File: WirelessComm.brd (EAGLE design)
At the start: 41.9 x 53.3 mm, 28 parts

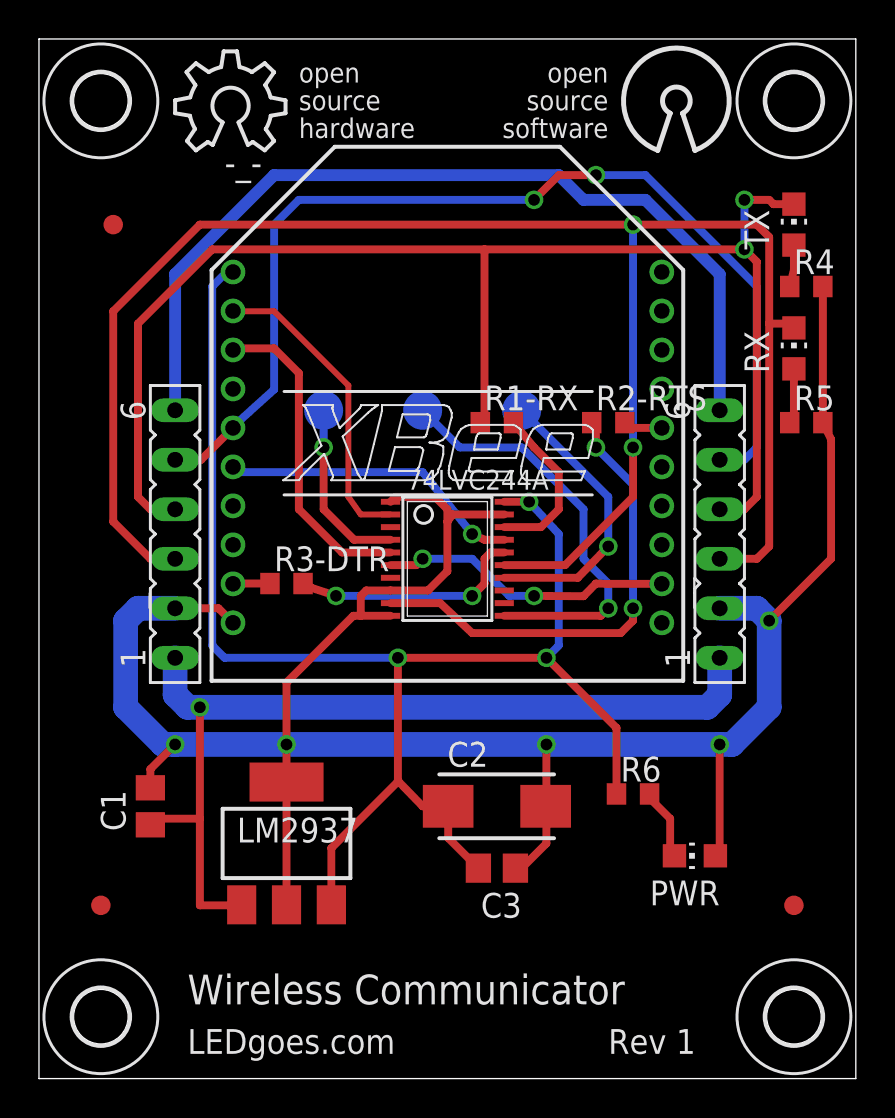
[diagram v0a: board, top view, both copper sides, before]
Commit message: First Production Revision
Passed design review check 2/25/14.  Rotated bee 90 degrees to keep this
board's size the same as the others.
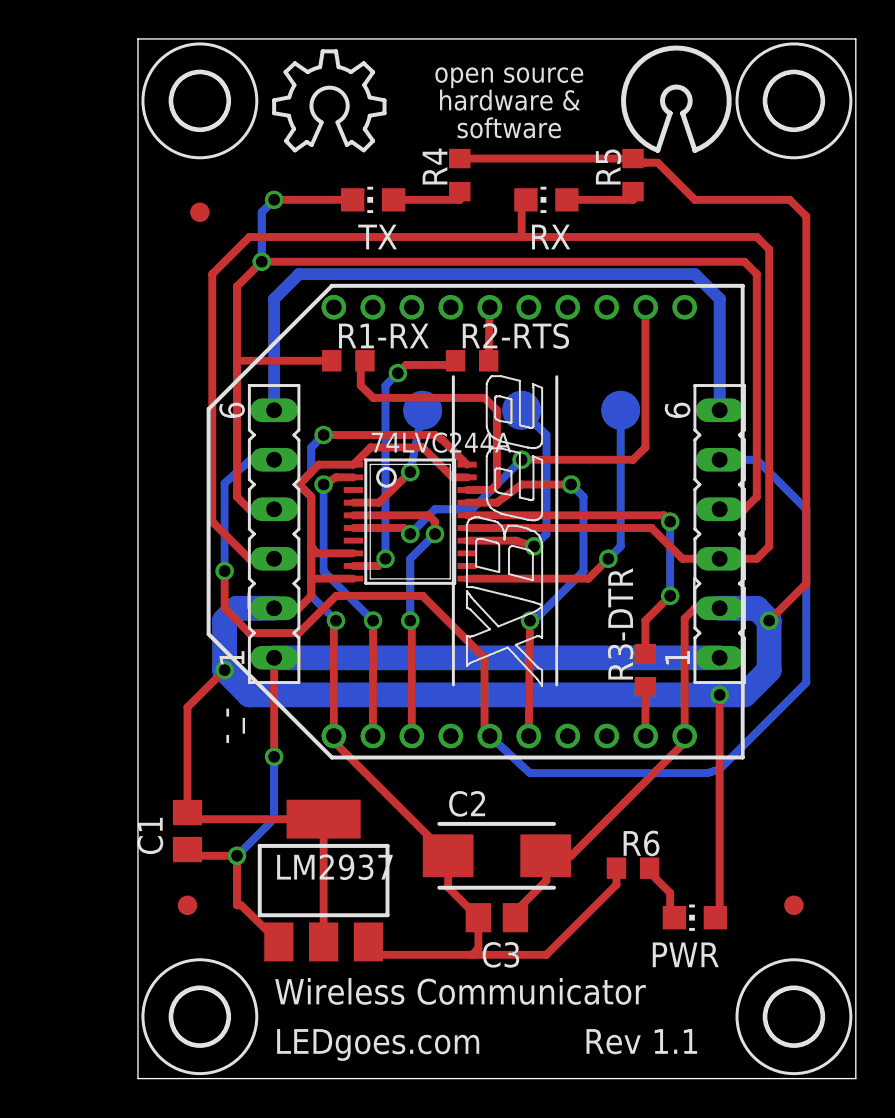
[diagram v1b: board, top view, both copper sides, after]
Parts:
- R4, R5, R6: value 47 -> 330
- moved TX 21.6 mm to (18.4, 42.5), turned to 90 degrees
- moved R3-DTR 18.9 mm to (32.4, 18.4), turned to 90 degrees
- moved R4 18.7 mm to (22.9, 43.8), turned to 90 degrees
- moved R5 15.5 mm to (31.8, 43.8), turned to 90 degrees
- moved RX 14.8 mm to (27.3, 42.5), turned to 90 degrees
- moved /RTS 10.2 mm to (31.1, 31.8)
- moved R1-RX 8.26 mm to (17.1, 34.3)
- moved R2-RTS 7.67 mm to (23.5, 34.3)
- moved E$1 5.08 mm to (13.3, 45.1)
- moved E$3 5.08 mm to (9.53, 47.6)
- moved E$4 5.08 mm to (9.53, 0.64)
- moved _ 5.08 mm to (13.3, 25.4)
- moved /DTR 5.08 mm to (21.0, 31.8)
- moved -_- 4.96 mm to (25.4, 26.0), turned to 90 degrees
- moved E$6 4.49 mm to (9.53, 41.9)
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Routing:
- net GND: track 126.8 -> 158.0 mm, vias 5 -> 3
- net S$3: track 76.8 -> 54.7 mm, vias 3 -> 2
- net S$23: track 93.0 -> 80.1 mm, vias 2 -> 0
- net S$1: track 46.1 -> 35.3 mm
- net S$13: track 24.4 -> 14.8 mm
- net S$10: track 15.1 -> 24.4 mm
- net S$2: track 53.6 -> 62.8 mm, vias 2 -> 1
- net VCC: track 50.3 -> 41.9 mm, vias 1 -> 2
- net S$25: track 73.2 -> 66.4 mm
- net S$7: track 8.53 -> 14.4 mm
- net S$4: track 21.5 -> 15.5 mm
- net S$15: track 12.1 -> 17.8 mm
- net S$16: track 15.8 -> 20.1 mm, vias 1 -> 2
- net S$5: track 14.8 -> 11.3 mm
- net S$17: track 9.16 -> 6.79 mm
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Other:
- board size 41.9 x 53.3 mm -> 36.8 x 53.3 mm
- board text added: "Rev 1.1"
- board text added: "open source hardware & software"
- board text removed: "Rev 1"
- board text removed: "open source hardware"
- board text removed: "open source software"

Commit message: Slight changes made to Rev 1 before production
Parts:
- turned PWR to 270 degrees
- turned RX to 270 degrees
- turned TX to 270 degrees
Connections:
- net GND: now also PWR.C; no longer PWR.A
- net S$11: now also PWR.A; no longer PWR.C
- net S$14: now also TX.C; no longer TX.A
- net S$18: now also RX.C; no longer RX.A
- net S$23: now also RX.A; no longer RX.C
- net S$25: now also TX.A; no longer TX.C
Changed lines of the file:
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@@
 <wire x1="43.18" y1="50.8" x2="6.35" y2="50.8" width="0" layer="20"/>
 <text x="13.335" y="-1.27" size="1.27" layer="25" font="vector">LEDgoes.com</text>
-<text x="10.16" y="17.78" size="0.8128" layer="26" font="vector" rot="MR90">VCC GND RX TX RST RIN</text>
+<text x="15.875" y="17.78" size="0.8128" layer="25" font="vector" rot="R90">VCC GND RX TX RST RIN</text>
 <text x="25.4" y="45.72" size="1.016" layer="25" font="vector" distance="40" align="bottom-center">open source
 hardware &amp;
@@
 <element name="E$2" library="holes" package="2,8" value="" x="40.005" y="47.625"/>
 <element name="E$5" library="holes" package="2,8" value="" x="40.005" y="0.635"/>
-<element name="-_-" library="maxstream" package="XBEE" value="" x="25.4" y="26.035" rot="R90"/>
-<element name="TX" library="led" package="CHIP-LED0805" value="" x="18.415" y="42.545" rot="R90"/>
-<element name="RX" library="led" package="CHIP-LED0805" value="" x="27.305" y="42.545" rot="R90"/>
-<element name="PWR" library="led" package="CHIP-LED0805" value="" x="34.925" y="5.715" rot="R90"/>
-<element name="74LVC244A" library="mcp2515" package="TSSOP20" value="" x="20.32" y="26.035" rot="R270"/>
-<element name="LM2937" library="v-reg" package="SOT223" value="" x="15.875" y="7.62"/>
-<element name="C1" library="eagle-ltspice" package="C0805" value="0.1uf" x="8.89" y="10.16" rot="R90"/>
-<element name="C3" library="eagle-ltspice" package="C0805" value="0.1uf" x="24.765" y="5.715" rot="R180"/>
-<element name="C2" library="resistor" package="CT6032" value="10uf" x="24.765" y="8.89"/>
-<element name="R3-DTR" library="eagle-ltspice" package="R0603" value="1k" x="32.385" y="18.415" rot="R90"/>
-<element name="R2-RTS" library="eagle-ltspice" package="R0603" value="1k" x="23.495" y="34.29"/>
-<element name="R1-RX" library="eagle-ltspice" package="R0603" value="1k" x="17.145" y="34.29"/>
-<element name="R4" library="eagle-ltspice" package="R0603" value="330" x="22.86" y="43.815" rot="R90"/>
-<element name="R5" library="eagle-ltspice" package="R0603" value="330" x="31.75" y="43.815" rot="R90"/>
-<element name="R6" library="eagle-ltspice" package="R0603" value="330" x="31.75" y="8.255"/>
+<element name="-_-" library="maxstream" package="XBEE" value="" x="25.4" y="26.035" smashed="yes" rot="R90">
+<attribute name="NAME" x="11.43" y="14.605" size="1.27" layer="25" rot="R90"/>
+<attribute name="VALUE" x="39.37" y="14.605" size="1.27" layer="27" rot="R90"/>
+</element>
+<element name="TX" library="led" package="CHIP-LED0805" value="" x="18.415" y="42.545" smashed="yes" rot="R270">
+<attribute name="NAME" x="17.78" y="43.815" size="1.016" layer="25" font="vector"/>
+<attribute name="VALUE" x="17.145" y="40.005" size="1.27" layer="27"/>
+</element>
+<element name="RX" library="led" package="CHIP-LED0805" value="" x="27.305" y="42.545" smashed="yes" rot="R270">
+<attribute name="NAME" x="26.67" y="40.64" size="1.016" layer="25" font="vector"/>
+<attribute name="VALUE" x="26.035" y="40.005" size="1.27" layer="27"/>
+</element>
+<element name="PWR" library="led" package="CHIP-LED0805" value="" x="34.925" y="5.715" smashed="yes" rot="R270">
+<attribute name="NAME" x="33.655" y="6.985" size="1.016" layer="25" font="vector"/>
+<attribute name="VALUE" x="33.655" y="3.175" size="1.27" layer="27"/>
+</element>
+<element name="74LVC244A" library="mcp2515" package="TSSOP20" value="" x="20.32" y="26.035" smashed="yes" rot="R270">
+<attribute name="NAME" x="18.2372" y="29.5806" size="1.016" layer="25" font="vector" ratio="10"/>
+<attribute name="VALUE" x="18.2372" y="21.4988" size="1.016" layer="27" ratio="10"/>
+</element>
+<element name="LM2937" library="v-reg" package="SOT223" value="" x="15.875" y="7.62" smashed="yes">
+<attribute name="NAME" x="13.335" y="12.1158" size="1.016" layer="25" font="vector"/>
+<attribute name="VALUE" x="13.335" y="6.2992" size="1.27" layer="27"/>
+</element>
+<element name="C1" library="eagle-ltspice" package="C0805" value="0.1uf" x="8.89" y="10.16" smashed="yes" rot="R90">
+<attribute name="NAME" x="7.62" y="9.525" size="1.016" layer="25" font="vector" rot="R90"/>
+<attribute name="VALUE" x="11.43" y="8.89" size="1.016" layer="27" font="vector" rot="R90"/>
+</element>
+<element name="C3" library="eagle-ltspice" package="C0805" value="0.1uf" x="24.765" y="5.715" smashed="yes" rot="R180">
+<attribute name="NAME" x="26.035" y="4.445" size="1.016" layer="25" font="vector" rot="R180"/>
+<attribute name="VALUE" x="26.035" y="8.255" size="1.016" layer="27" font="vector" rot="R180"/>
+</element>
+<element name="C2" library="resistor" package="CT6032" value="10uf" x="24.765" y="8.89" smashed="yes">
+<attribute name="NAME" x="24.13" y="10.922" size="1.016" layer="25" font="vector"/>
+<attribute name="VALUE" x="22.225" y="5.715" size="1.016" layer="27" font="vector"/>
+</element>
+<element name="R3-DTR" library="eagle-ltspice" package="R0603" value="1k" x="32.385" y="18.415" smashed="yes" rot="R90">
+<attribute name="NAME" x="31.75" y="16.51" size="1.016" layer="25" font="vector" rot="R90"/>
+<attribute name="VALUE" x="34.29" y="17.78" size="1.016" layer="27" font="vector" rot="R90"/>
+</element>
+<element name="R2-RTS" library="eagle-ltspice" package="R0603" value="1k" x="23.495" y="34.29" smashed="yes">
+<attribute name="NAME" x="20.955" y="34.925" size="1.016" layer="25" font="vector"/>
+<attribute name="VALUE" x="22.86" y="32.385" size="1.016" layer="27" font="vector"/>
+</element>
+<element name="R1-RX" library="eagle-ltspice" package="R0603" value="1k" x="17.145" y="34.29" smashed="yes">
+<attribute name="NAME" x="15.24" y="34.925" size="1.016" layer="25" font="vector"/>
+<attribute name="VALUE" x="16.51" y="32.385" size="1.016" layer="27" font="vector"/>
+</element>
+<element name="R4" library="eagle-ltspice" package="R0603" value="330" x="22.86" y="43.815" smashed="yes" rot="R90">
+<attribute name="NAME" x="22.225" y="43.18" size="1.016" layer="25" font="vector" rot="R90"/>
+<attribute name="VALUE" x="24.765" y="43.18" size="1.016" layer="27" font="vector" rot="R90"/>
+</element>
+<element name="R5" library="eagle-ltspice" package="R0603" value="330" x="31.75" y="43.815" smashed="yes" rot="R90">
+<attribute name="NAME" x="31.115" y="43.18" size="1.016" layer="25" font="vector" rot="R90"/>
+<attribute name="VALUE" x="33.655" y="43.18" size="1.016" layer="27" font="vector" rot="R90"/>
+</element>
+<element name="R6" library="eagle-ltspice" package="R0603" value="330" x="31.75" y="8.255" smashed="yes">
+<attribute name="NAME" x="31.115" y="8.89" size="1.016" layer="25" font="vector"/>
+<attribute name="VALUE" x="30.48" y="6.35" size="1.016" layer="27" font="vector"/>
+</element>
 <element name="E$8" library="adafruit" package="FIDUCIAL_1MM" value="" x="40.005" y="6.35"/>
 <element name="/CTS" library="testpad" package="TP20R" value="" x="26.035" y="31.75" rot="MR90"/>
@@
 <contactref element="C1" pad="2"/>
 <contactref element="-_-" pad="10"/>
-<contactref element="PWR" pad="A"/>
 <contactref element="R5" pad="2"/>
 <via x="36.195" y="17.145" extent="1-16" drill="0.6"/>
-<wire x1="36.195" y1="17.145" x2="36.195" y2="5.935" width="0.4064" layer="1"/>
-<wire x1="36.195" y1="5.935" x2="35.975" y2="5.715" width="0.4064" layer="1"/>
+<wire x1="36.195" y1="17.145" x2="36.195" y2="5.715" width="0.4064" layer="1"/>
 <via x="38.735" y="20.955" extent="1-16" drill="0.6"/>
 <wire x1="38.735" y1="20.955" x2="40.64" y2="22.86" width="0.4064" layer="1"/>
@@
 <wire x1="27.305" y1="7.62" x2="27.305" y2="8.85" width="0.4064" layer="1"/>
 <wire x1="27.305" y1="8.85" x2="27.265" y2="8.89" width="0.4064" layer="1"/>
+<contactref element="PWR" pad="C"/>
+<wire x1="35.975" y1="5.715" x2="36.195" y2="5.715" width="0.4064" layer="1"/>
 </signal>
 <signal name="S$6">
@@
 <wire x1="32.695" y1="25.71" x2="34.29" y2="24.13" width="0.4064" layer="1"/>
 <wire x1="34.29" y1="24.13" x2="36.195" y2="24.13" width="0.4064" layer="1"/>
-<contactref element="RX" pad="C"/>
+<contactref element="RX" pad="A"/>
 <wire x1="26.255" y1="42.545" x2="26.035" y2="42.545" width="0.4064" layer="1"/>
 <wire x1="26.035" y1="42.545" x2="26.035" y2="40.64" width="0.4064" layer="1"/>
@@
 <wire x1="13.335" y1="42.545" x2="12.7" y2="41.91" width="0.4064" layer="16"/>
 <wire x1="12.7" y1="41.91" x2="12.7" y2="39.37" width="0.4064" layer="16"/>
-<contactref element="TX" pad="C"/>
 <contactref element="R1-RX" pad="1"/>
 <wire x1="16.295" y1="34.29" x2="11.43" y2="34.29" width="0.4064" layer="1"/>
-<wire x1="13.335" y1="42.545" x2="17.365" y2="42.545" width="0.4064" layer="1"/>
+<contactref element="TX" pad="A"/>
+<wire x1="17.365" y1="42.545" x2="13.335" y2="42.545" width="0.4064" layer="1"/>
 </signal>
 <signal name="S$10">
@@
 </signal>
 <signal name="S$11">
-<contactref element="PWR" pad="C"/>
 <contactref element="R6" pad="2"/>
 <wire x1="32.6" y1="8.255" x2="32.6" y2="8.04" width="0.4064" layer="1"/>
 <wire x1="32.6" y1="8.04" x2="33.655" y2="6.985" width="0.4064" layer="1"/>
-<wire x1="33.655" y1="6.985" x2="33.655" y2="5.935" width="0.4064" layer="1"/>
-<wire x1="33.655" y1="5.935" x2="33.875" y2="5.715" width="0.4064" layer="1"/>
+<contactref element="PWR" pad="A"/>
+<wire x1="33.875" y1="5.715" x2="33.655" y2="5.715" width="0.4064" layer="1"/>
+<wire x1="33.655" y1="5.715" x2="33.655" y2="6.985" width="0.4064" layer="1"/>
 </signal>
 <signal name="S$18">
-<contactref element="RX" pad="A"/>
 <contactref element="R5" pad="1"/>
+<contactref element="RX" pad="C"/>
 <wire x1="28.355" y1="42.545" x2="31.75" y2="42.545" width="0.4064" layer="1"/>
 <wire x1="31.75" y1="42.545" x2="31.75" y2="42.965" width="0.4064" layer="1"/>
@@
 <signal name="S$14">
 <contactref element="R4" pad="1"/>
-<contactref element="TX" pad="A"/>
+<contactref element="TX" pad="C"/>
 <wire x1="19.465" y1="42.545" x2="22.86" y2="42.545" width="0.4064" layer="1"/>
 <wire x1="22.86" y1="42.545" x2="22.86" y2="42.965" width="0.4064" layer="1"/>
